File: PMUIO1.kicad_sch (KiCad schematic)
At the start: 24 parts, among them J2 USB_OTG, Q1 Q_PNP_BEC, U1 rv1126/rv1109

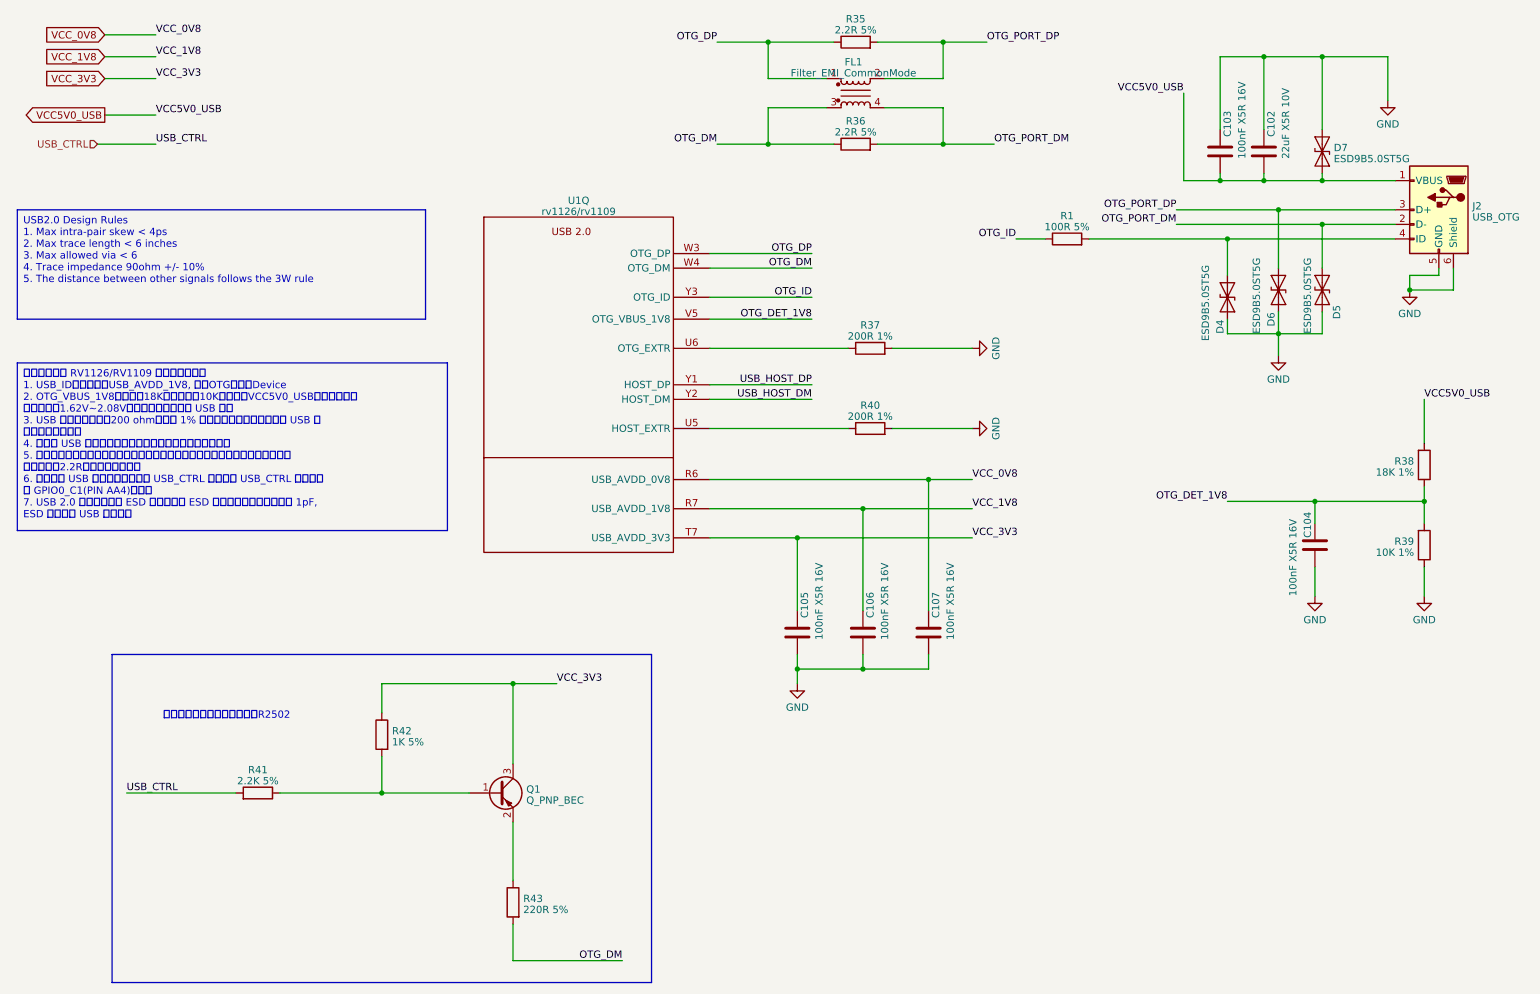
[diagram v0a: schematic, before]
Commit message: updated USB
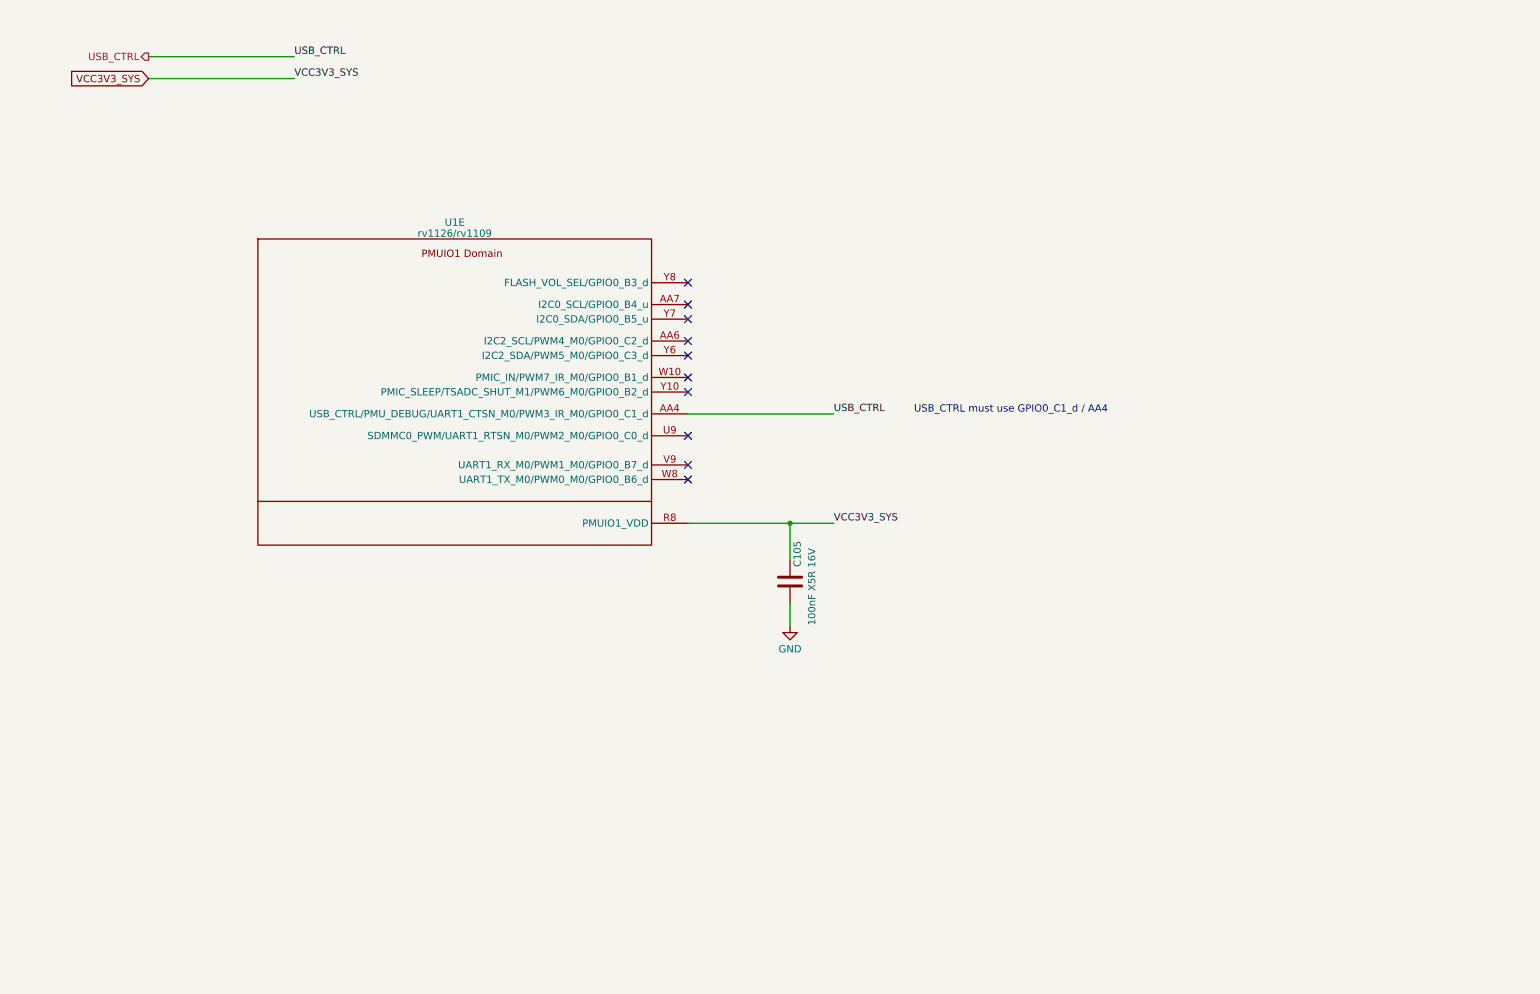
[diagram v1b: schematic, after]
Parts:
- removed C102: 22uF X5R 10V, Capacitor_SMD:C_0805_2012Metric, symbol Device:C
- removed C103, C104: 100nF X5R 16V, Capacitor_SMD:C_0402_1005Metric, symbol Device:C
- removed C106, C107: 100nF X5R 16V, Capacitor_SMD:C_0201_0603Metric, symbol Device:C
- removed D4, D5, D6, D7: ESD9B5.0ST5G, Diode_SMD:D_SOD-923, symbol Diode:ESD9B5.0ST5G
- removed FL1: Filter_EMI_CommonMode, Inductor_SMD:L_CommonModeChoke_Coilcraft_0603USB, symbol Device:Filter_EMI_CommonMode
- removed J2: USB_OTG, symbol Connector:USB_OTG
- removed Q1: Q_PNP_BEC, Package_TO_SOT_SMD:SOT-23, symbol Device:Q_PNP_BEC
- removed R1: 100R 5%, Resistor_SMD:R_0402_1005Metric, symbol Device:R
- removed R35, R36: 2.2R 5%, Resistor_SMD:R_0603_1608Metric, symbol Device:R
- removed R37, R40: 200R 1%, Resistor_SMD:R_0402_1005Metric, symbol Device:R
- removed R38: 18K 1%, Resistor_SMD:R_0402_1005Metric, symbol Device:R
- removed R39: 10K 1%, Resistor_SMD:R_0402_1005Metric, symbol Device:R
- removed R41: 2.2K 5%, Resistor_SMD:R_0402_1005Metric, symbol Device:R
- removed R42: 1K 5%, Resistor_SMD:R_0402_1005Metric, symbol Device:R
- removed R43: 220R 5%, Resistor_SMD:R_0402_1005Metric, symbol Device:R
- removed U1: rv1126/rv1109, symbol CPU_Rockchip:rv1126_rv1109
- added U1: rv1126/rv1109, symbol CPU_Rockchip:rv1126_rv1109
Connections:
- net USB_CTRL: now also U1.AA4 (USB_CTRL/PMU_DEBUG/UART1_CTSN_M0/PWM3_IR_M0/GPIO0_C1_d)
- net VCC_3V3 renamed VCC3V3_SYS
- net VCC3V3_SYS: now also U1.R8 (PMUIO1_VDD)
- no-connect marks 0 -> 10
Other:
- note added: "USB_CTRL must use GPIO0_C1_d / AA4"
- note removed: "参考设计中需要将此电路靠近R2502"
- company: Qingdao IotPi Information Technology -> (none)
- title: Leaf RV1126 RK809 USB OTG -> (none)

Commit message: link FLASH_VOL_SEL
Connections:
- net FLASH_VOL_SEL: now reaches U1.Y8 (FLASH_VOL_SEL/GPIO0_B3_d)
- no-connect marks 10 -> 9
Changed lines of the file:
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@@
   (no_connect (at 133.35 97.79))
   (no_connect (at 133.35 80.01))
-  (no_connect (at 133.35 63.5))
   (no_connect (at 133.35 90.17))
   (no_connect (at 133.35 82.55))
   (no_connect (at 133.35 69.85))
+  (wire (pts (xy 39.37 34.29) (xy 64.77 34.29))
+    (stroke (width 0) (type default))
+  )
   (wire (pts (xy 133.35 86.36) (xy 158.75 86.36))
     (stroke (width 0) (type default))
@@
     (stroke (width 0) (type default))
   )
+  (wire (pts (xy 133.35 63.5) (xy 139.7 63.5))
+    (stroke (width 0) (type default))
+  )
   (text "USB_CTRL must use GPIO0_C1_d / AA4" (at 172.72 86.36 0)
+    (effects (font (size 1.27 1.27)) (justify left bottom))
+  )
+  (label "FLASH_VOL_SEL" (at 64.77 34.29 0) (fields_autoplaced)
     (effects (font (size 1.27 1.27)) (justify left bottom))
   )
@@
     (effects (font (size 1.27 1.27)) (justify left bottom))
   )
+  (label "FLASH_VOL_SEL" (at 139.7 63.5 0) (fields_autoplaced)
+    (effects (font (size 1.27 1.27)) (justify left bottom))
+  )
   (label "USB_CTRL" (at 64.77 24.13 0) (fields_autoplaced)
     (effects (font (size 1.27 1.27)) (justify left bottom))
@@
     )
   )
+  (hierarchical_label "FLASH_VOL_SEL" (shape input) (at 39.37 34.29 180) (fields_autoplaced)
+    (effects (font (size 1.27 1.27)) (justify right))
+  )
   (hierarchical_label "USB_CTRL" (shape output) (at 39.37 24.13 180) (fields_autoplaced)

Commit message: updated footprints
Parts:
- U1: footprint (none) -> Rockchip_SoC:Rockchip_RV1126_FCCSP409LD_14.0x14.0mm
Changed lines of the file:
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@@
         )
         (path "/e3b58043-16a3-43c8-9fad-9c9784eebfa4/74154bd6-827c-4e46-8351-0d1a22db546e"
-          (reference "C108") (unit 1)
+          (reference "C140") (unit 1)
         )
       )
@@
       (effects (font (size 1.27 1.27)))
     )
-    (property "Footprint" "" (at 125.73 107.95 0)
+    (property "Footprint" "Rockchip_SoC:Rockchip_RV1126_FCCSP409LD_14.0x14.0mm" (at 125.73 107.95 0)
       (effects (font (size 1.27 1.27)) hide)
     )
@@
   (symbol (lib_id "power:GND") (at 151.13 123.19 0) (unit 1)
     (in_bom yes) (on_board yes) (dnp no) (fields_autoplaced)
-    (property "Reference" "#PWR085" (at 151.13 129.54 0)
+    (property "Reference" "#PWR0128" (at 151.13 129.54 0)
       (effects (font (size 1.27 1.27)) hide)
     )
@@
       (project "leaf"
         (path "/e3b58043-16a3-43c8-9fad-9c9784eebfa4/74154bd6-827c-4e46-8351-0d1a22db546e"
-          (reference "#PWR085") (unit 1)
+          (reference "#PWR0128") (unit 1)
         )
       )

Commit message: updated Capacitors
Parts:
- C105: value 100nF X5R 16V -> 100nF X5R 6.3V; LCSC (none) -> C76934; Model (none) -> GRM033R61A104KE15D; Vendor (none) -> muRata(村田)
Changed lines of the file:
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@@
       (effects (font (size 1.27 1.27)) (justify left))
     )
-    (property "Value" "100nF X5R 16V" (at 154.94 123.19 90)
+    (property "Value" "100nF X5R 6.3V" (at 154.94 123.19 90)
       (effects (font (size 1.27 1.27)) (justify left))
     )
@@
       (effects (font (size 1.27 1.27)) hide)
     )
+    (property "Description" "容值: 100nF 精度: ±10% 额定电压: 10V 材质(温度系数): X5R 材质:X5R" (at 151.13 115.57 0)
+      (effects (font (size 1.27 1.27)) hide)
+    )
+    (property "Model" "GRM033R61A104KE15D" (at 151.13 115.57 0)
+      (effects (font (size 1.27 1.27)) hide)
+    )
+    (property "Vendor" "muRata(村田)" (at 151.13 115.57 0)
+      (effects (font (size 1.27 1.27)) hide)
+    )
+    (property "LCSC" "C76934" (at 151.13 115.57 0)
+      (effects (font (size 1.27 1.27)) hide)
+    )

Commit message: layout SoC Power and DDR capacitors
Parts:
- C105: LCSC C76934 -> C76928; Model GRM033R61A104KE15D -> GRM033R60J104KE19D
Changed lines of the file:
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@@
       (effects (font (size 1.27 1.27)) hide)
     )
-    (property "Description" "容值: 100nF 精度: ±10% 额定电压: 10V 材质(温度系数): X5R 材质:X5R" (at 151.13 115.57 0)
+    (property "Description" "容值: 100nF 精度: ±10% 额定电压: 6.3V 材质(温度系数): X5R 材质:X5R" (at 151.13 115.57 0)
       (effects (font (size 1.27 1.27)) hide)
     )
-    (property "Model" "GRM033R61A104KE15D" (at 151.13 115.57 0)
+    (property "Model" "GRM033R60J104KE19D" (at 151.13 115.57 0)
       (effects (font (size 1.27 1.27)) hide)
     )
@@
       (effects (font (size 1.27 1.27)) hide)
     )
-    (property "LCSC" "C76934" (at 151.13 115.57 0)
+    (property "LCSC" "C76928" (at 151.13 115.57 0)
       (effects (font (size 1.27 1.27)) hide)
     )

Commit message: fix some ERCs
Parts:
- renumbered C105 to C?
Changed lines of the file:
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@@
   (symbol (lib_id "Device:C") (at 151.13 115.57 0) (unit 1)
     (in_bom yes) (on_board yes) (dnp no)
-    (property "Reference" "C105" (at 152.4 113.03 90)
+    (property "Reference" "C?" (at 152.4 113.03 90)
       (effects (font (size 1.27 1.27)) (justify left))
     )
@@
       (project "leaf"
         (path "/e3b58043-16a3-43c8-9fad-9c9784eebfa4/be5d8e43-2411-4620-a7a9-8dc1a750f993"
-          (reference "C105") (unit 1)
+          (reference "C?") (unit 1)
         )
         (path "/e3b58043-16a3-43c8-9fad-9c9784eebfa4/74154bd6-827c-4e46-8351-0d1a22db546e"
-          (reference "C140") (unit 1)
+          (reference "C136") (unit 1)
         )
       )
@@
     (pin "Y21")
     (pin "C21")
-    (pin "D20")
     (pin "D21")
     (pin "E19")
@@
   (symbol (lib_id "power:GND") (at 151.13 123.19 0) (unit 1)
     (in_bom yes) (on_board yes) (dnp no) (fields_autoplaced)
-    (property "Reference" "#PWR0128" (at 151.13 129.54 0)
+    (property "Reference" "#PWR0127" (at 151.13 129.54 0)
       (effects (font (size 1.27 1.27)) hide)
     )
@@
       (project "leaf"
         (path "/e3b58043-16a3-43c8-9fad-9c9784eebfa4/74154bd6-827c-4e46-8351-0d1a22db546e"
-          (reference "#PWR0128") (unit 1)
+          (reference "#PWR0127") (unit 1)
         )
       )
